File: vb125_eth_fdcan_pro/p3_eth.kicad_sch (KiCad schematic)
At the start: 40 parts, among them J2 ARJM11C7-114-BA-EW2, U2 LAN8740A, X1 50MHz

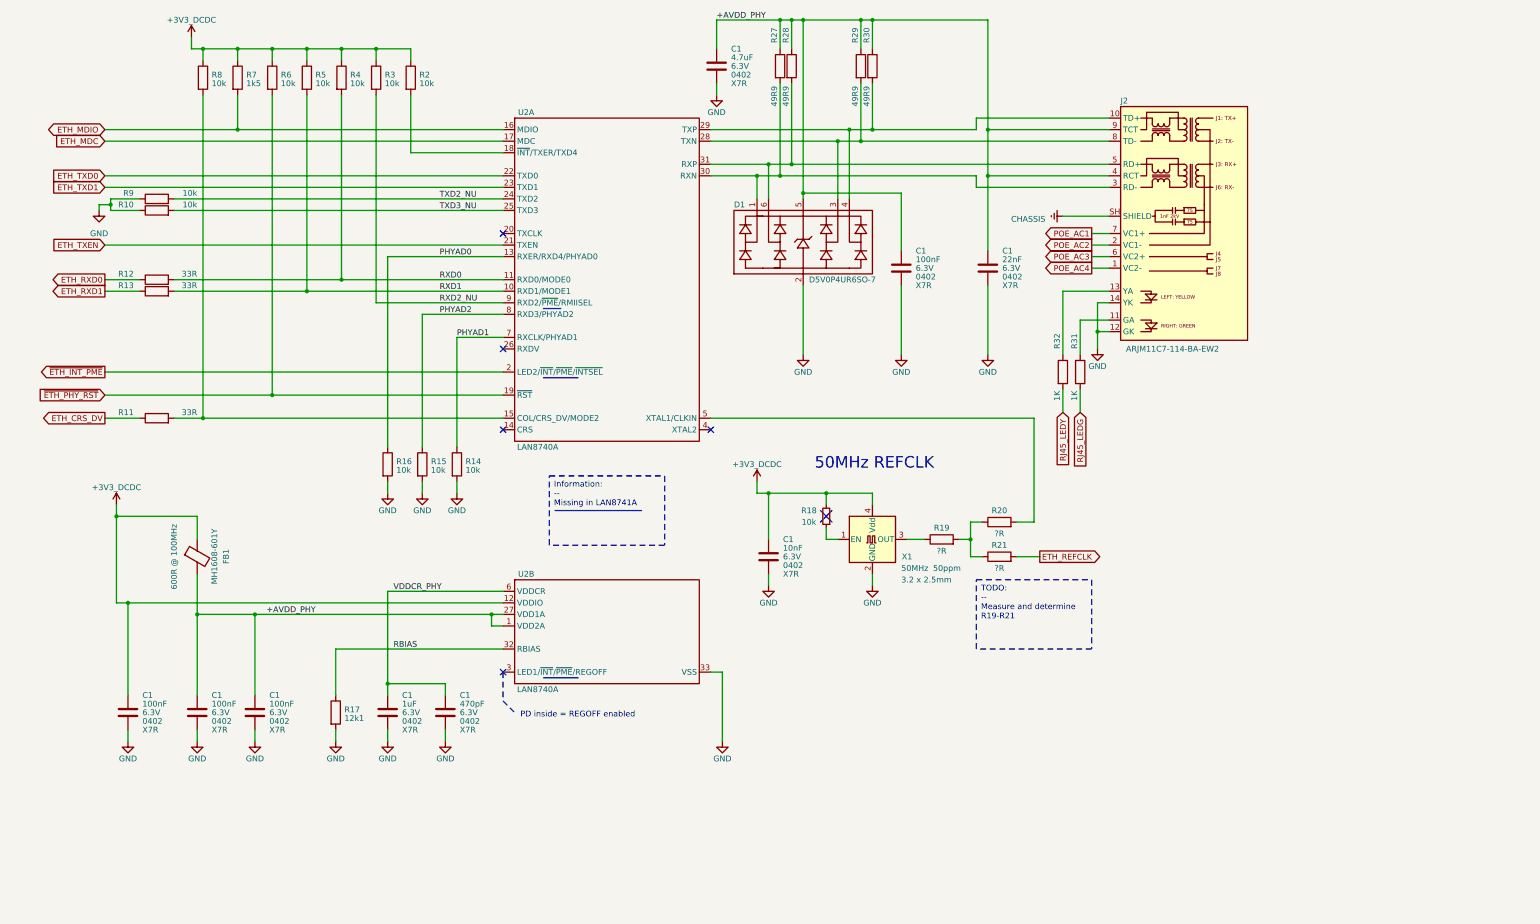
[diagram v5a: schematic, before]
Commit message: Add testpoints and set page templates.
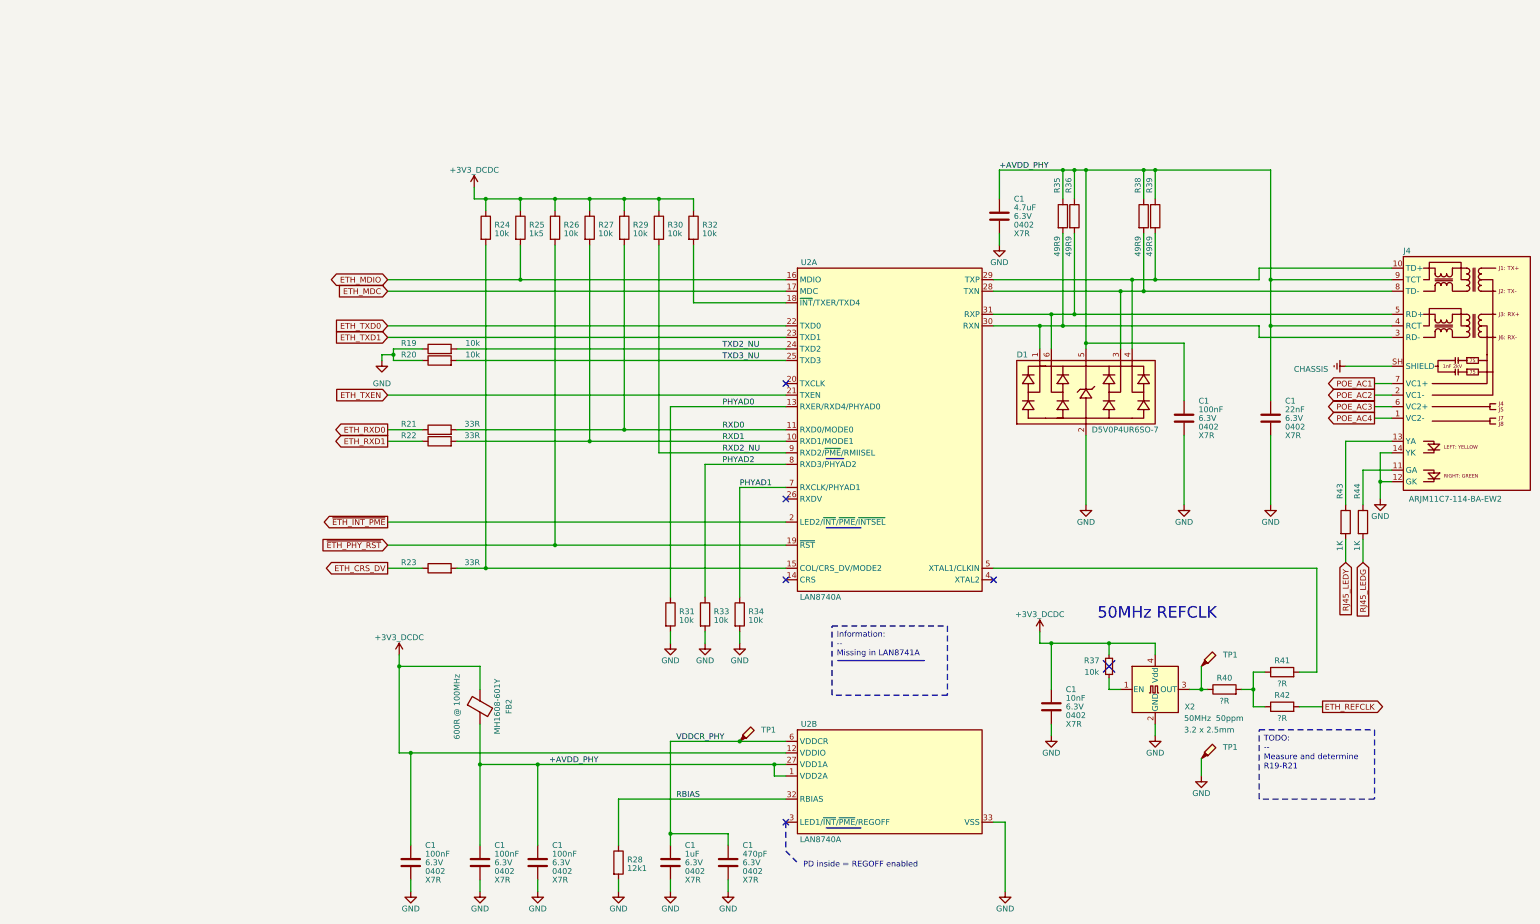
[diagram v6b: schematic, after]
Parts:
- added TP1 (x3): TestPoint_Probe, TestPoint:TestPoint_Pad_D1.5mm, symbol Connector:TestPoint_Probe
- renumbered FB1 to FB2, J2 to J4, R9 to R19, R10 to R20, R12 to R21, R13 to R22, R11 to R23, R8 to R24, R7 to R25, R6 to R26, R5 to R27, R17 to R28, R4 to R29, R3 to R30, R16 to R31, R2 to R32, R15 to R33, R14 to R34, R27 to R35, R28 to R36, R18 to R37, R29 to R38, R30 to R39, R19 to R40, R20 to R41, R21 to R42, R32 to R43, R31 to R44, X1 to X2
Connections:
- net GND: now also TP1.1
- net VDDCR_PHY: now also TP1.1
- net at R40.1, X2.3 (OUT): now also TP1.1
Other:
- company: (none) -> vhrd.tech AS
- title: (none) -> rt_bridge_pro
- moved on the sheet: C1, FB2, J4, R19, R20, R21, R22, R23, R24, R25, R26, R27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

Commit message: Add sourcing information for resistors
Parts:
- R19, R20, R24, R26, R27, R29, R30, R31, R32, R33, R34, R37: Mpn1 (none) -> RMCF0402FT10K0; Mpn2 (none) -> CR0402-FX-1002GLF
- R21, R22, R23: Mpn1 (none) -> CR0402-FX-33R0GLF; Mpn2 (none) -> RMCF0402FT33R0
- R25: Mpn1 (none) -> CR0402-FX-1501GLF; Mpn2 (none) -> RMCF0402FT1K50
- R28: Mpn1 (none) -> RMCF0402FT12K1; Mpn2 (none) -> RC0402FR-0712K1L
- R35, R36, R38, R39: Mpn1 (none) -> CR0402-FX-49R9GLF; Mpn2 (none) -> RMCF0402FT49R9
- R43, R44: Mpn1 (none) -> RMCF0402FT1K00; Mpn2 (none) -> RC0402FR-071KL
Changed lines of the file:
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@@
+      (effects (font (size 1.27 1.27)) hide)
+    )
+    (property "Mpn1" "CR0402-FX-49R9GLF" (at 240.03 68.58 0)
+      (effects (font (size 1.27 1.27)) hide)
+    )
+    (property "Mpn2" "RMCF0402FT49R9" (at 240.03 68.58 0)
       (effects (font (size 1.27 1.27)) hide)
     )
@@
     )
     (property "Datasheet" "~" (at 257.81 68.58 0)
+      (effects (font (size 1.27 1.27)) hide)
+    )
+    (property "Mpn1" "CR0402-FX-49R9GLF" (at 257.81 68.58 0)
+      (effects (font (size 1.27 1.27)) hide)
+    )
+    (property "Mpn2" "RMCF0402FT49R9" (at 257.81 68.58 0)
       (effects (font (size 1.27 1.27)) hide)
     )
@@
     )
     (property "Datasheet" "~" (at 302.26 135.89 0)
+      (effects (font (size 1.27 1.27)) hide)
+    )
+    (property "Mpn1" "RMCF0402FT1K00" (at 302.26 135.89 0)
+      (effects (font (size 1.27 1.27)) hide)
+    )
+    (property "Mpn2" "RC0402FR-071KL" (at 302.26 135.89 0)
       (effects (font (size 1.27 1.27)) hide)
     )
@@
       (effects (font (size 1.27 1.27)) hide)
     )
+    (property "Mpn1" "CR0402-FX-33R0GLF" (at 102.87 118.11 0)
+      (effects (font (size 1.27 1.27)) hide)
+    )
+    (property "Mpn2" "RMCF0402FT33R0" (at 102.87 118.11 0)
+      (effects (font (size 1.27 1.27)) hide)
+    )
     (pin "1")
     (pin "2")
@@
       (effects (font (size 1.27 1.27)) hide)
     )
+    (property "Mpn1" "CR0402-FX-33R0GLF" (at 102.87 146.05 0)
+      (effects (font (size 1.27 1.27)) hide)
+    )
+    (property "Mpn2" "RMCF0402FT33R0" (at 102.87 146.05 0)
+      (effects (font (size 1.27 1.27)) hide)
+    )
     (pin "1")
     (pin "2")
@@
       (effects (font (size 1.27 1.27)) hide)
     )
+    (property "Mpn1" "RMCF0402FT10K0" (at 113.03 71.12 0)
+      (effects (font (size 1.27 1.27)) hide)
+    )
+    (property "Mpn2" "CR0402-FX-1002GLF" (at 113.03 71.12 0)
+      (effects (font (size 1.27 1.27)) hide)
+    )
     (pin "1")
     (pin "2")
@@
       (effects (font (size 1.27 1.27)) hide)
     )
+    (property "Mpn1" "RMCF0402FT10K0" (at 102.87 100.33 0)
+      (effects (font (size 1.27 1.27)) hide)
+    )
+    (property "Mpn2" "CR0402-FX-1002GLF" (at 102.87 100.33 0)
+      (effects (font (size 1.27 1.27)) hide)
+    )
     (pin "1")
     (pin "2")
@@
       (effects (font (size 1.27 1.27)) hide)
     )
+    (property "Mpn1" "RMCF0402FT10K0" (at 158.75 71.12 0)
+      (effects (font (size 1.27 1.27)) hide)
+    )
+    (property "Mpn2" "CR0402-FX-1002GLF" (at 158.75 71.12 0)
+      (effects (font (size 1.27 1.27)) hide)
+    )
     (pin "1")
     (pin "2")
@@
     )
     (property "Datasheet" "~" (at 260.35 68.58 0)
+      (effects (font (size 1.27 1.27)) hide)
+    )
+    (property "Mpn1" "CR0402-FX-49R9GLF" (at 260.35 68.58 0)
+      (effects (font (size 1.27 1.27)) hide)
+    )
+    (property "Mpn2" "RMCF0402FT49R9" (at 260.35 68.58 0)
       (effects (font (size 1.27 1.27)) hide)
     )
@@
       (effects (font (size 1.27 1.27)) hide)
     )
+    (property "Mpn1" "CR0402-FX-33R0GLF" (at 102.87 115.57 0)
+      (effects (font (size 1.27 1.27)) hide)
+    )
+    (property "Mpn2" "RMCF0402FT33R0" (at 102.87 115.57 0)
+      (effects (font (size 1.27 1.27)) hide)
+    )
     (pin "1")
     (pin "2")
@@
     )
     (property "Datasheet" "~" (at 143.51 71.12 0)
+      (effects (font (size 1.27 1.27)) hide)
+    )
+    (property "Mpn1" "RMCF0402FT10K0" (at 143.51 71.12 0)
+      (effects (font (size 1.27 1.27)) hide)
+    )
+    (property "Mpn2" "CR0402-FX-1002GLF" (at 143.51 71.12 0)
       (effects (font (size 1.27 1.27)) hide)
     )
@@
       (effects (font (size 1.27 1.27)) hide)
     )
+    (property "Mpn1" "RMCF0402FT10K0" (at 161.29 156.21 0)
+      (effects (font (size 1.27 1.27)) hide)
+    )
+    (property "Mpn2" "CR0402-FX-1002GLF" (at 161.29 156.21 0)
+      (effects (font (size 1.27 1.27)) hide)
+    )
     (pin "1")
     (pin "2")
@@
     )
     (property "Datasheet" "~" (at 306.07 135.89 0)
+      (effects (font (size 1.27 1.27)) hide)
+    )
+    (property "Mpn1" "RMCF0402FT1K00" (at 306.07 135.89 0)
+      (effects (font (size 1.27 1.27)) hide)
+    )
+    (property "Mpn2" "RC0402FR-071KL" (at 306.07 135.89 0)
       (effects (font (size 1.27 1.27)) hide)
     )
@@
       (effects (font (size 1.27 1.27)) hide)
     )
+    (property "Mpn1" "RMCF0402FT12K1" (at 142.24 210.82 0)
+      (effects (font (size 1.27 1.27)) hide)
+    )
+    (property "Mpn2" "RC0402FR-0712K1L" (at 142.24 210.82 0)
+      (effects (font (size 1.27 1.27)) hide)
+    )
     (pin "1")
     (pin "2")
@@
     )
     (property "Datasheet" "~" (at 102.87 97.79 0)
+      (effects (font (size 1.27 1.27)) hide)
+    )
+    (property "Mpn1" "RMCF0402FT10K0" (at 102.87 97.79 0)
+      (effects (font (size 1.27 1.27)) hide)
+    )
+    (property "Mpn2" "CR0402-FX-1002GLF" (at 102.87 97.79 0)
       (effects (font (size 1.27 1.27)) hide)
     )
@@
       (effects (font (size 1.27 1.27)) hide)
     )
+    (property "Mpn1" "CR0402-FX-49R9GLF" (at 242.57 68.58 0)
+      (effects (font (size 1.27 1.27)) hide)
+    )
+    (property "Mpn2" "RMCF0402FT49R9" (at 242.57 68.58 0)
+      (effects (font (size 1.27 1.27)) hide)
+    )
     (pin "1")
     (pin "2")
@@
       (effects (font (size 1.27 1.27)) hide)
     )
+    (property "Mpn1" "RMCF0402FT10K0" (at 153.67 156.21 0)
+      (effects (font (size 1.27 1.27)) hide)
+    )
+    (property "Mpn2" "CR0402-FX-1002GLF" (at 153.67 156.21 0)
+      (effects (font (size 1.27 1.27)) hide)
+    )
     (pin "1")
     (pin "2")
@@
       (effects (font (size 1.27 1.27)) hide)
     )
+    (property "Mpn1" "CR0402-FX-1501GLF" (at 120.65 71.12 0)
+      (effects (font (size 1.27 1.27)) hide)
+    )
+    (property "Mpn2" "RMCF0402FT1K50" (at 120.65 71.12 0)
+      (effects (font (size 1.27 1.27)) hide)
+    )
     (pin "1")
     (pin "2")
@@
       (effects (font (size 1.27 1.27)) hide)
     )
+    (property "Mpn1" "RMCF0402FT10K0" (at 135.89 71.12 0)
+      (effects (font (size 1.27 1.27)) hide)
+    )
+    (property "Mpn2" "CR0402-FX-1002GLF" (at 135.89 71.12 0)
+      (effects (font (size 1.27 1.27)) hide)
+    )
     (pin "1")
     (pin "2")
@@
     )
     (property "Datasheet" "~" (at 151.13 71.12 0)
+      (effects (font (size 1.27 1.27)) hide)
+    )
+    (property "Mpn1" "RMCF0402FT10K0" (at 151.13 71.12 0)
+      (effects (font (size 1.27 1.27)) hide)
+    )
+    (property "Mpn2" "CR0402-FX-1002GLF" (at 151.13 71.12 0)
       (effects (font (size 1.27 1.27)) hide)
     )
@@
       (effects (font (size 1.27 1.27)) hide)
     )
+    (property "Mpn1" "RMCF0402FT10K0" (at 128.27 71.12 0)
+      (effects (font (size 1.27 1.27)) hide)
+    )
+    (property "Mpn2" "CR0402-FX-1002GLF" (at 128.27 71.12 0)
+      (effects (font (size 1.27 1.27)) hide)
+    )
     (pin "1")
     (pin "2")
@@
       (effects (font (size 1.27 1.27)) hide)
     )
+    (property "Mpn1" "RMCF0402FT10K0" (at 250.19 167.64 0)
+      (effects (font (size 1.27 1.27)) hide)
+    )
+    (property "Mpn2" "CR0402-FX-1002GLF" (at 250.19 167.64 0)
+      (effects (font (size 1.27 1.27)) hide)
+    )
     (pin "1")
     (pin "2")
@@
       (effects (font (size 1.27 1.27)) hide)
     )
+    (property "Mpn1" "RMCF0402FT10K0" (at 168.91 156.21 0)
+      (effects (font (size 1.27 1.27)) hide)
+    )
+    (property "Mpn2" "CR0402-FX-1002GLF" (at 168.91 156.21 0)
+      (effects (font (size 1.27 1.27)) hide)
+    )

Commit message: Selection of capacitors for VB125
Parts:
- C1: Mpn1 (none) -> GRM155R70J223KA01J; Mpn2 (none) -> C0402C223K9RAC7867
- C1: Mpn1 (none) -> Samsung:CL05B104KQ5NNNC; Mpn2 (none) -> YAGEO:CC0402KRX7R5BB104
- C1: Mpn1 (none) -> Murata:GRM155R70J105KA12D; Mpn2 (none) -> Murata:GRM155R70J105KA12J
- C1: Mpn1 (none) -> C0402C471K9RAC7867; Mpn2 (none) -> 1 ПРОИЗВ. В 0402 И 1 ПРОИЗВ. В 0603
- C1: Mpn1 (none) -> 0402B103K6R3CT; Mpn2 (none) -> 04026C103KAT2A
- C1: Mpn1 (none) -> 06036C475KAT2A; Mpn2 (none) -> ТОЛЬКО ОДИН ПРОИЗВОДИТ. В КОРПУСЕ 0603
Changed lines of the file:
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@@
       (effects (font (size 1.27 1.27)) (justify left))
+    )
+    (property "Mpn1" "GRM155R70J223KA01J" (at 285.75 113.03 0)
+      (effects (font (size 1.27 1.27)) hide)
+    )
+    (property "Mpn2" "C0402C223K9RAC7867" (at 285.75 113.03 0)
+      (effects (font (size 1.27 1.27)) hide)
     )
     (pin "1")
@@
       (effects (font (size 1.27 1.27)) (justify left))
     )
+    (property "Mpn1" "Samsung:CL05B104KQ5NNNC  " (at 266.7 113.03 0)
+      (effects (font (size 1.27 1.27)) hide)
+    )
+    (property "Mpn2" "YAGEO:CC0402KRX7R5BB104" (at 266.7 113.03 0)
+      (effects (font (size 1.27 1.27)) hide)
+    )
     (pin "1")
     (pin "2")
@@
       (effects (font (size 1.27 1.27)) hide)
     )
+    (property "Mpn1" "Murata:GRM155R70J105KA12D" (at 153.67 210.82 0)
+      (effects (font (size 1.27 1.27)) hide)
+    )
+    (property "Mpn2" "Murata:GRM155R70J105KA12J" (at 153.67 210.82 0)
+      (effects (font (size 1.27 1.27)) hide)
+    )
     (pin "1")
     (pin "2")
@@
       (effects (font (size 1.27 1.27)) hide)
     )
+    (property "Mpn1" "Samsung:CL05B104KQ5NNNC  " (at 124.46 210.82 0)
+      (effects (font (size 1.27 1.27)) hide)
+    )
+    (property "Mpn2" "YAGEO:CC0402KRX7R5BB104" (at 124.46 210.82 0)
+      (effects (font (size 1.27 1.27)) hide)
+    )
     (pin "1")
     (pin "2")
@@
     )
     (property "Vworking" "3.3V" (at 111.76 210.82 0)
+      (effects (font (size 1.27 1.27)) hide)
+    )
+    (property "Mpn1" "Samsung:CL05B104KQ5NNNC  " (at 111.76 210.82 0)
+      (effects (font (size 1.27 1.27)) hide)
+    )
+    (property "Mpn2" "YAGEO:CC0402KRX7R5BB104" (at 111.76 210.82 0)
       (effects (font (size 1.27 1.27)) hide)
     )
@@
       (effects (font (size 1.27 1.27)) hide)
     )
+    (property "Mpn1" "C0402C471K9RAC7867" (at 166.37 210.82 0)
+      (effects (font (size 1.27 1.27)) hide)
+    )
+    (property "Mpn2" "1 ПРОИЗВ. В 0402 И 1 ПРОИЗВ. В 0603" (at 166.37 210.82 0)
+      (effects (font (size 1.27 1.27)) hide)
+    )
     (pin "1")
     (pin "2")
@@
     )
     (property "Vworking" "3.3V" (at 96.52 210.82 0)
+      (effects (font (size 1.27 1.27)) hide)
+    )
+    (property "Mpn1" "Samsung:CL05B104KQ5NNNC  " (at 96.52 210.82 0)
+      (effects (font (size 1.27 1.27)) hide)
+    )
+    (property "Mpn2" "YAGEO:CC0402KRX7R5BB104" (at 96.52 210.82 0)
       (effects (font (size 1.27 1.27)) hide)
     )
@@
     )
     (property "Vworking" "3.3V" (at 237.49 176.53 0)
+      (effects (font (size 1.27 1.27)) hide)
+    )
+    (property "Mpn1" "0402B103K6R3CT" (at 237.49 176.53 0)
+      (effects (font (size 1.27 1.27)) hide)
+    )
+    (property "Mpn2" "04026C103KAT2A" (at 237.49 176.53 0)
       (effects (font (size 1.27 1.27)) hide)
     )
@@
       (effects (font (size 1.27 1.27)) (justify left))
     )
-    (pin "1")
+    (property "Mpn1" "06036C475KAT2A" (at 226.06 68.58 0)
+      (effects (font (size 1.27 1.27)) hide)
+    )
+    (property "Mpn2" "ТОЛЬКО ОДИН ПРОИЗВОДИТ. В КОРПУСЕ 0603" (at 226.06 68.58 0)
+      (effects (font (size 1.27 1.27)) hide)
+    )
+    (pin "1")
